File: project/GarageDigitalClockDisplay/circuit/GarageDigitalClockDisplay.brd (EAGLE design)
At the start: 200.7 x 78.7 mm, 124 parts

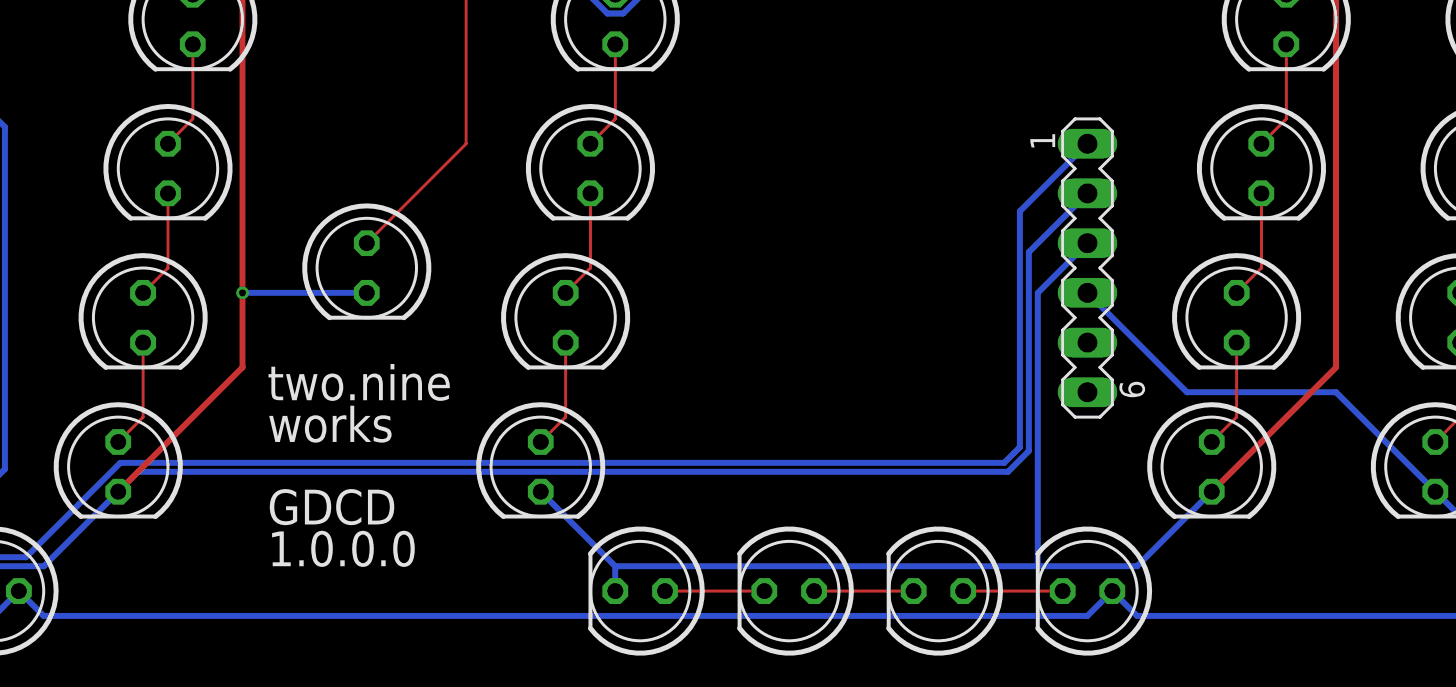
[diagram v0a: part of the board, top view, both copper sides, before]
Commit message: コントローラのピッチを変更
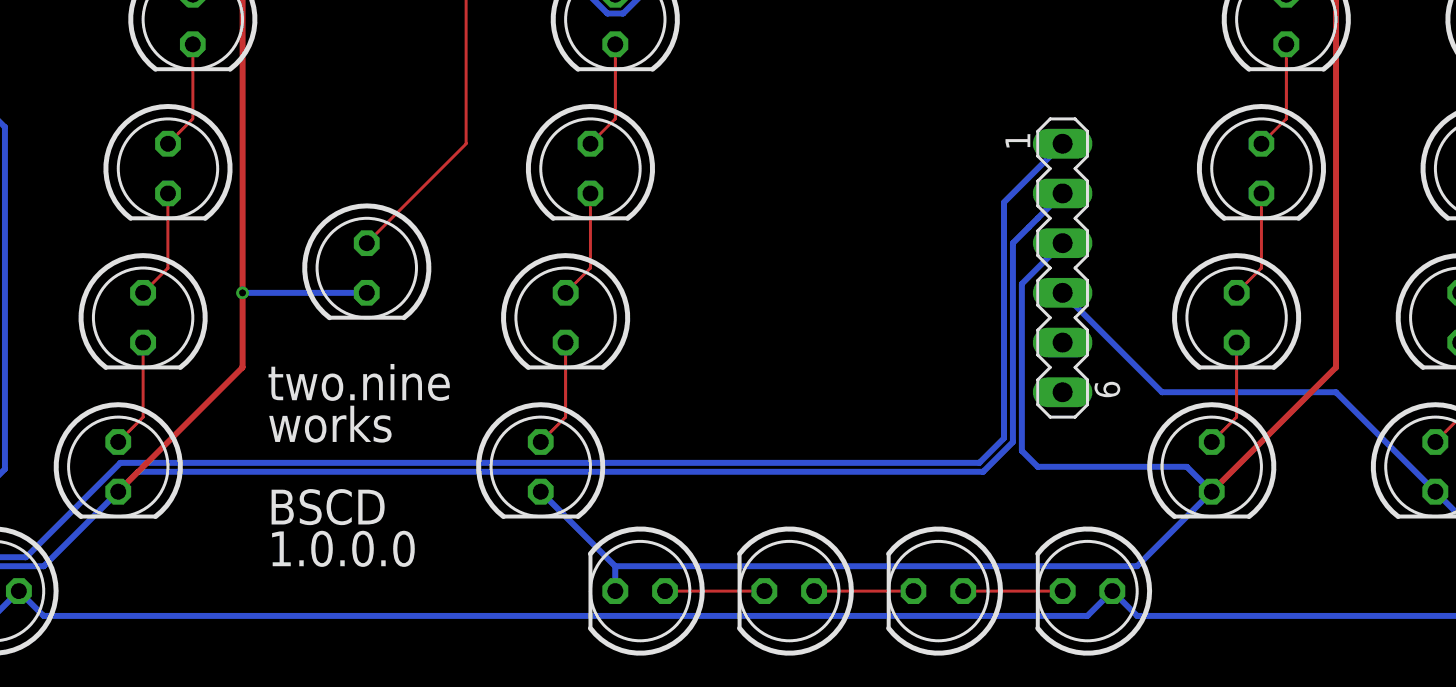
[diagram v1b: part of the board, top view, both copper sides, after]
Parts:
- moved SV2 1.27 mm to (133.3, 21.6)
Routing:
- net N$89: track 168.6 -> 173.1 mm
- net N$58: track 219.2 -> 217.9 mm
- net N$118: track 173.0 -> 174.3 mm
- net N$29: track 264.3 -> 263.0 mm
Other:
- board text added: "BSCD 1.0.0.0"
- board text removed: "GDCD 1.0.0.0"
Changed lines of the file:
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@@
 <?xml version="1.0" encoding="utf-8"?>
 <!DOCTYPE eagle SYSTEM "eagle.dtd">
-<eagle version="9.6.1">
+<eagle version="9.6.2">
 <drawing>
 <settings>
@@
 <text x="92.71" y="12.7" size="1.778" layer="21" distance="20">two.nine
 works</text>
-<text x="92.71" y="6.35" size="1.778" layer="21" distance="20">GDCD
+<text x="92.71" y="6.35" size="1.778" layer="21" distance="20">BSCD
 1.0.0.0</text>
 </plain>
@@
 <attribute name="VALUE" x="56.769" y="22.86" size="1.27" layer="27" ratio="10" rot="R270"/>
 </element>
-<element name="SV2" library="con-lstb" library_urn="urn:adsk.eagle:library:162" package="MA06-1" package3d_urn="urn:adsk.eagle:package:8340/1" value="" x="134.62" y="21.59" smashed="yes" rot="R270">
-<attribute name="MF" value="" x="130.81" y="-21.59" size="1.778" layer="27" rot="R270" display="off"/>
-<attribute name="MPN" value="" x="130.81" y="-21.59" size="1.778" layer="27" rot="R270" display="off"/>
-<attribute name="OC_FARNELL" value="unknown" x="130.81" y="-21.59" size="1.778" layer="27" rot="R270" display="off"/>
-<attribute name="OC_NEWARK" value="unknown" x="130.81" y="-21.59" size="1.778" layer="27" rot="R270" display="off"/>
-<attribute name="POPULARITY" value="28" x="130.81" y="-21.59" size="1.778" layer="27" rot="R270" display="off"/>
-<attribute name="VALUE" x="131.699" y="24.13" size="1.27" layer="27" ratio="10" rot="R270"/>
+<element name="SV2" library="con-lstb" library_urn="urn:adsk.eagle:library:162" package="MA06-1" package3d_urn="urn:adsk.eagle:package:8340/1" value="" x="133.35" y="21.59" smashed="yes" rot="R270">
+<attribute name="MF" value="" x="129.54" y="-21.59" size="1.778" layer="27" rot="R270" display="off"/>
+<attribute name="MPN" value="" x="129.54" y="-21.59" size="1.778" layer="27" rot="R270" display="off"/>
+<attribute name="OC_FARNELL" value="unknown" x="129.54" y="-21.59" size="1.778" layer="27" rot="R270" display="off"/>
+<attribute name="OC_NEWARK" value="unknown" x="129.54" y="-21.59" size="1.778" layer="27" rot="R270" display="off"/>
+<attribute name="POPULARITY" value="28" x="129.54" y="-21.59" size="1.778" layer="27" rot="R270" display="off"/>
+<attribute name="VALUE" x="130.429" y="24.13" size="1.27" layer="27" ratio="10" rot="R270"/>
 </element>
 </elements>
@@
 <wire x1="51.1998" y1="11.1252" x2="40.3352" y2="11.1252" width="0.3048" layer="16"/>
 <wire x1="40.3352" y1="11.1252" x2="39.37" y2="10.16" width="0.3048" layer="16"/>
-<wire x1="134.62" y1="27.94" x2="131.1656" y2="24.4856" width="0.3048" layer="16"/>
-<wire x1="131.1656" y1="12.43218125" x2="131.121709375" y2="12.388290625" width="0.3048" layer="16"/>
-<wire x1="131.121709375" y1="12.388290625" x2="130.867709375" y2="12.134290625" width="0.3048" layer="16"/>
-<wire x1="131.1656" y1="24.4856" x2="131.1656" y2="12.43218125" width="0.3048" layer="16"/>
-<wire x1="130.867709375" y1="12.134290625" x2="130.36661875" y2="11.6332" width="0.3048" layer="16"/>
-<wire x1="130.36661875" y1="11.6332" x2="85.1982" y2="11.6332" width="0.3048" layer="16"/>
+<wire x1="129.09661875" y1="11.6332" x2="85.1982" y2="11.6332" width="0.3048" layer="16"/>
+<wire x1="133.35" y1="27.94" x2="130.3528" y2="24.9428" width="0.3048" layer="16"/>
+<wire x1="130.3528" y1="24.9428" x2="130.3528" y2="12.88938125" width="0.3048" layer="16"/>
+<wire x1="130.3528" y1="12.88938125" x2="129.09661875" y2="11.6332" width="0.3048" layer="16"/>
 <wire x1="85.1982" y1="11.6332" x2="80.3722" y2="6.8072" width="0.3048" layer="16"/>
 </signal>
@@
 <wire x1="54.61" y1="67.31" x2="60.96" y2="73.66" width="0.3048" layer="1"/>
 <wire x1="60.96" y1="73.66" x2="64.77" y2="73.66" width="0.3048" layer="1"/>
-<wire x1="131.6228" y1="12.2428" x2="130.556" y2="11.176" width="0.3048" layer="16"/>
 <wire x1="86.106" y1="11.176" x2="85.09" y2="10.16" width="0.3048" layer="16"/>
-<wire x1="134.62" y1="25.4" x2="131.6228" y2="22.4028" width="0.3048" layer="16"/>
-<wire x1="131.6228" y1="22.4028" x2="131.6228" y2="12.2428" width="0.3048" layer="16"/>
-<wire x1="130.556" y1="11.176" x2="86.106" y2="11.176" width="0.3048" layer="16"/>
+<wire x1="133.35" y1="25.4" x2="132.08" y2="24.13" width="0.3048" layer="16"/>
 <via x="91.44" y="20.32" extent="1-16" drill="0.35"/>
+<wire x1="132.08" y1="24.13" x2="131.6228" y2="23.6728" width="0.3048" layer="16"/>
 <wire x1="97.79" y1="20.32" x2="91.44" y2="20.32" width="0.3048" layer="16"/>
+<wire x1="131.6228" y1="23.6728" x2="130.81" y2="22.86" width="0.3048" layer="16"/>
+<wire x1="130.81" y1="22.86" x2="130.81" y2="12.7" width="0.3048" layer="16"/>
+<wire x1="130.81" y1="12.7" x2="129.286" y2="11.176" width="0.3048" layer="16"/>
+<wire x1="129.286" y1="11.176" x2="86.106" y2="11.176" width="0.3048" layer="16"/>
 </signal>
 <signal name="N$59">
@@
 <wire x1="110.49" y1="6.35" x2="110.49" y2="5.08" width="0.3048" layer="16"/>
 <wire x1="140.97" y1="10.16" x2="137.16" y2="6.35" width="0.3048" layer="16"/>
-<wire x1="137.16" y1="6.35" x2="132.08" y2="6.35" width="0.3048" layer="16"/>
-<wire x1="132.08" y1="6.35" x2="110.49" y2="6.35" width="0.3048" layer="16"/>
+<wire x1="137.16" y1="6.35" x2="110.49" y2="6.35" width="0.3048" layer="16"/>
 <wire x1="146.05" y1="44.45" x2="147.32" y2="43.18" width="0.3048" layer="1"/>
 <wire x1="147.32" y1="16.51" x2="140.97" y2="10.16" width="0.3048" layer="1"/>
@@
 <wire x1="110.49" y1="67.31" x2="116.84" y2="73.66" width="0.3048" layer="1"/>
 <wire x1="116.84" y1="73.66" x2="120.65" y2="73.66" width="0.3048" layer="1"/>
-<wire x1="134.62" y1="22.86" x2="132.08" y2="20.32" width="0.3048" layer="16"/>
-<wire x1="132.08" y1="20.32" x2="132.08" y2="6.35" width="0.3048" layer="16"/>
+<wire x1="131.2672" y1="12.2428" x2="132.08" y2="11.43" width="0.3048" layer="16"/>
+<wire x1="132.08" y1="11.43" x2="139.7" y2="11.43" width="0.3048" layer="16"/>
+<wire x1="139.7" y1="11.43" x2="140.97" y2="10.16" width="0.3048" layer="16"/>
+<wire x1="133.35" y1="22.86" x2="131.2672" y2="20.7772" width="0.3048" layer="16"/>
+<wire x1="131.2672" y1="20.7772" x2="131.2672" y2="12.2428" width="0.3048" layer="16"/>
 </signal>
 <signal name="N$90">
@@
 <wire x1="156.21" y1="67.31" x2="162.56" y2="73.66" width="0.3048" layer="1"/>
 <wire x1="162.56" y1="73.66" x2="166.37" y2="73.66" width="0.3048" layer="1"/>
-<wire x1="134.62" y1="20.32" x2="139.7" y2="15.24" width="0.3048" layer="16"/>
-<wire x1="139.7" y1="15.24" x2="147.32" y2="15.24" width="0.3048" layer="16"/>
+<wire x1="133.35" y1="20.32" x2="138.43" y2="15.24" width="0.3048" layer="16"/>
+<wire x1="138.43" y1="15.24" x2="147.32" y2="15.24" width="0.3048" layer="16"/>
 <wire x1="147.32" y1="15.24" x2="152.4" y2="10.16" width="0.3048" layer="16"/>
 </signal>
